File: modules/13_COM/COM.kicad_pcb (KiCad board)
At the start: 2 copper layers, 160 x 100 mm, 52 parts, among them J1 Card_Connector, J3 GATE LED, J4 IS INPUT, J5 OUT 1, J6 OUT 2, P1 4k7, P2 100k, P3 100k, P4 100k, P5 250k, U1 RC4136

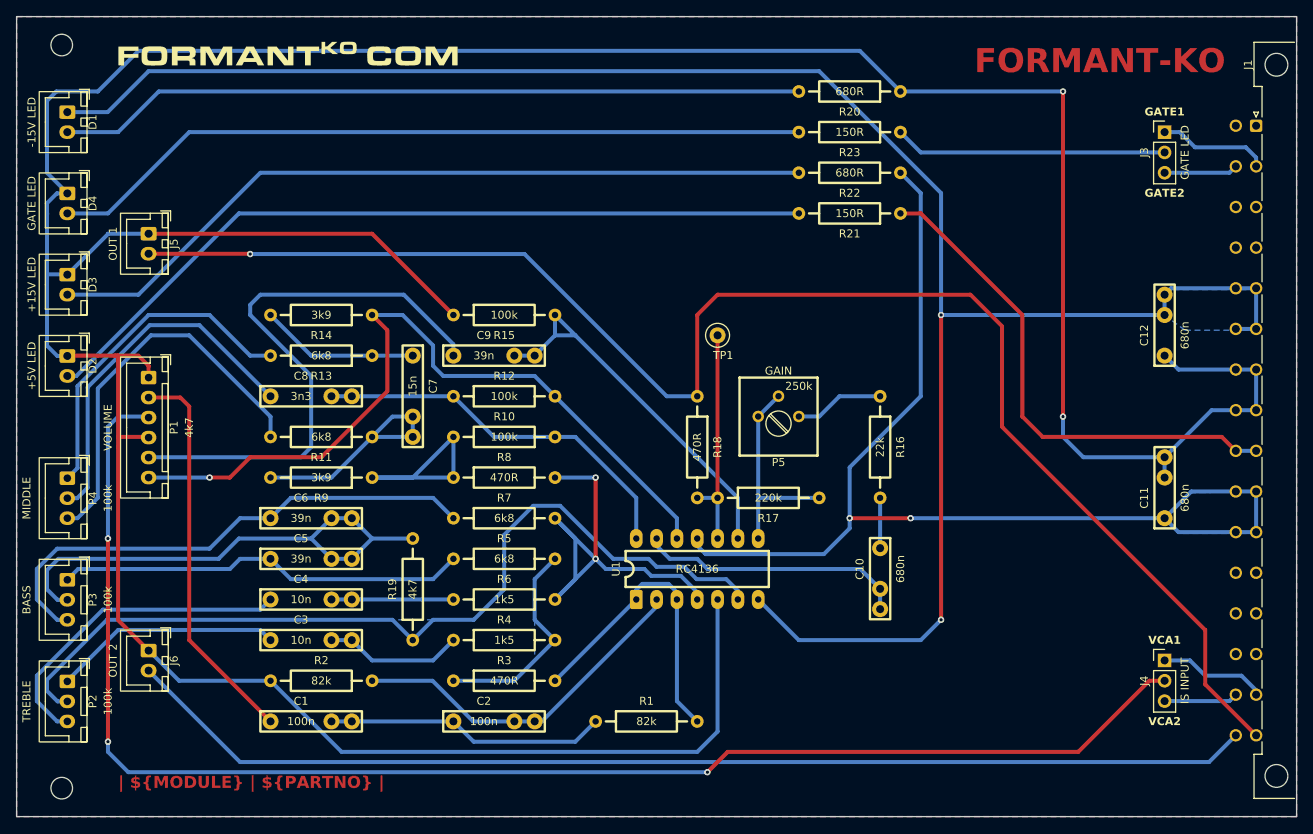
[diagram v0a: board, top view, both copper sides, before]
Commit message: COM updates, NPD text
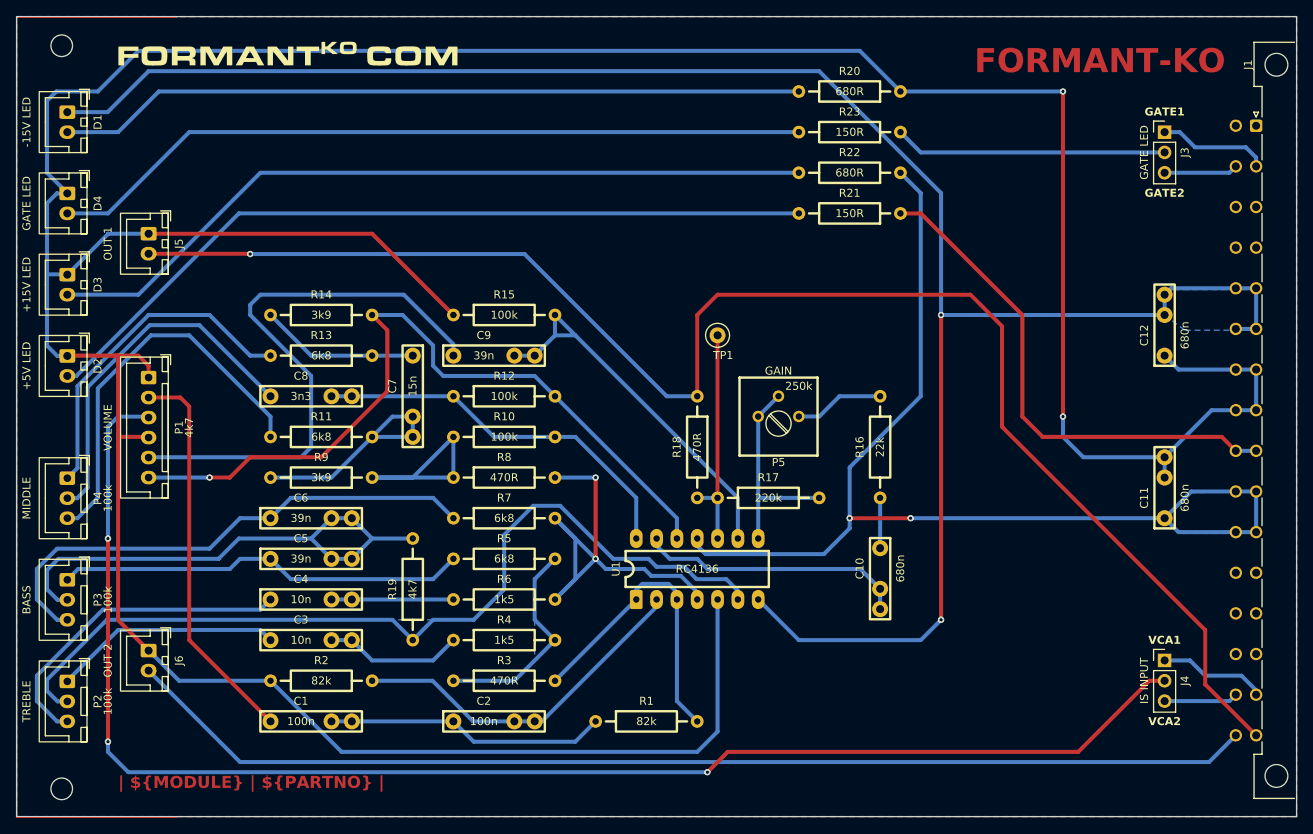
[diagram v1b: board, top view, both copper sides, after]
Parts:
- D1: value -15V LED -> Panel_LED
- D2: value +5V LED -> Panel_LED
- D3: value +15V LED -> Panel_LED
- D4: value GATE LED -> Panel_LED
- J5: value OUT 1 -> Mono_Jack
- J6: value OUT 2 -> Mono_Jack
- moved MH1 0.09 mm to (55.0, 45.1)

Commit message: com work
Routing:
- added copper zone on B.Cu, net Net-(R17-Pad1)

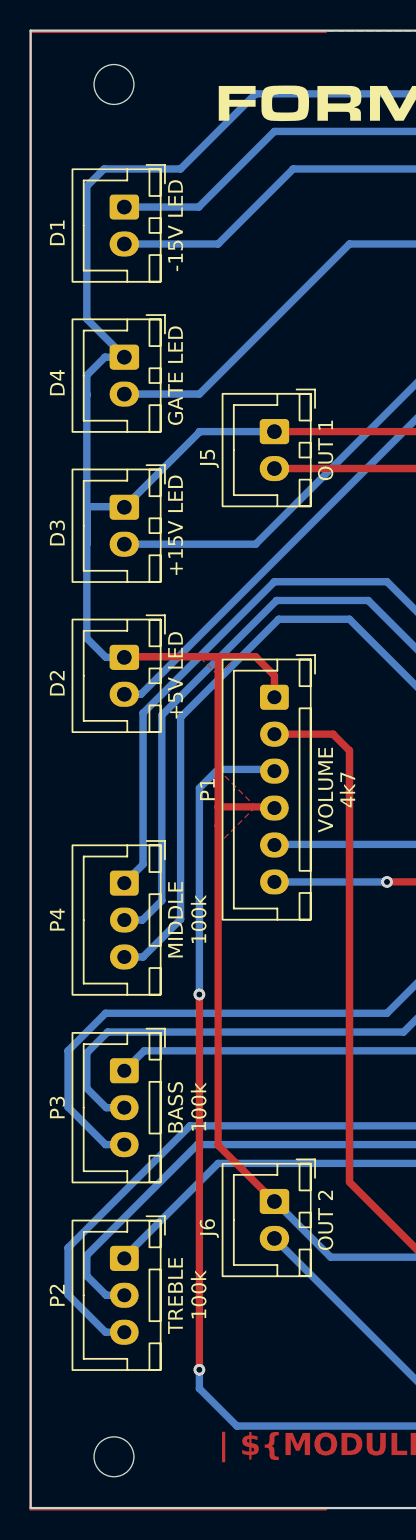
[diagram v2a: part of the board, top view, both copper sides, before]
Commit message: fixed card bracket footprint
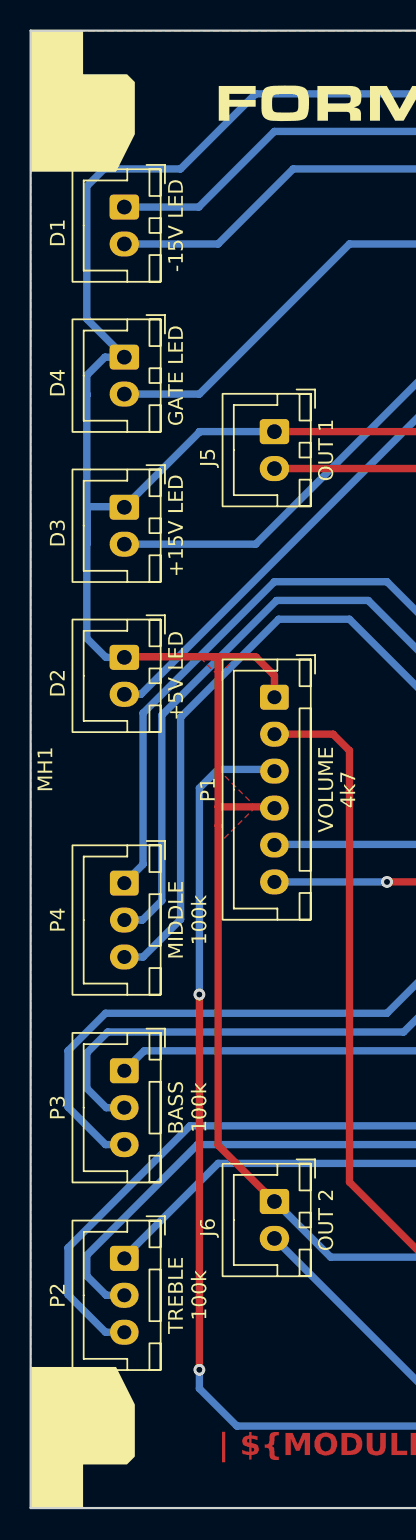
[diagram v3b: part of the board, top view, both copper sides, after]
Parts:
- MH1: value ~ -> CardBracket; footprint FormantKO:Schroff_60807-011_3U_Pair -> FormantKO:Card_Bracket
- moved MH1 49.9 mm to (55.0, 95.0)
